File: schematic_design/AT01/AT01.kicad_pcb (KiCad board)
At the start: 2 copper layers, 36 parts, among them J1 JST Connector, J2 Conn_01x04_Pin, M2 Motor_DC (Pump), M3 Motor_DC (Solenoid), P1 USB_C_Plug_USB2.0, Q1 DMG2301L, SW1 SW_Push, U1 MPRLS0025PA00001A, U2 FT232RL, U3 DRV8833PW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

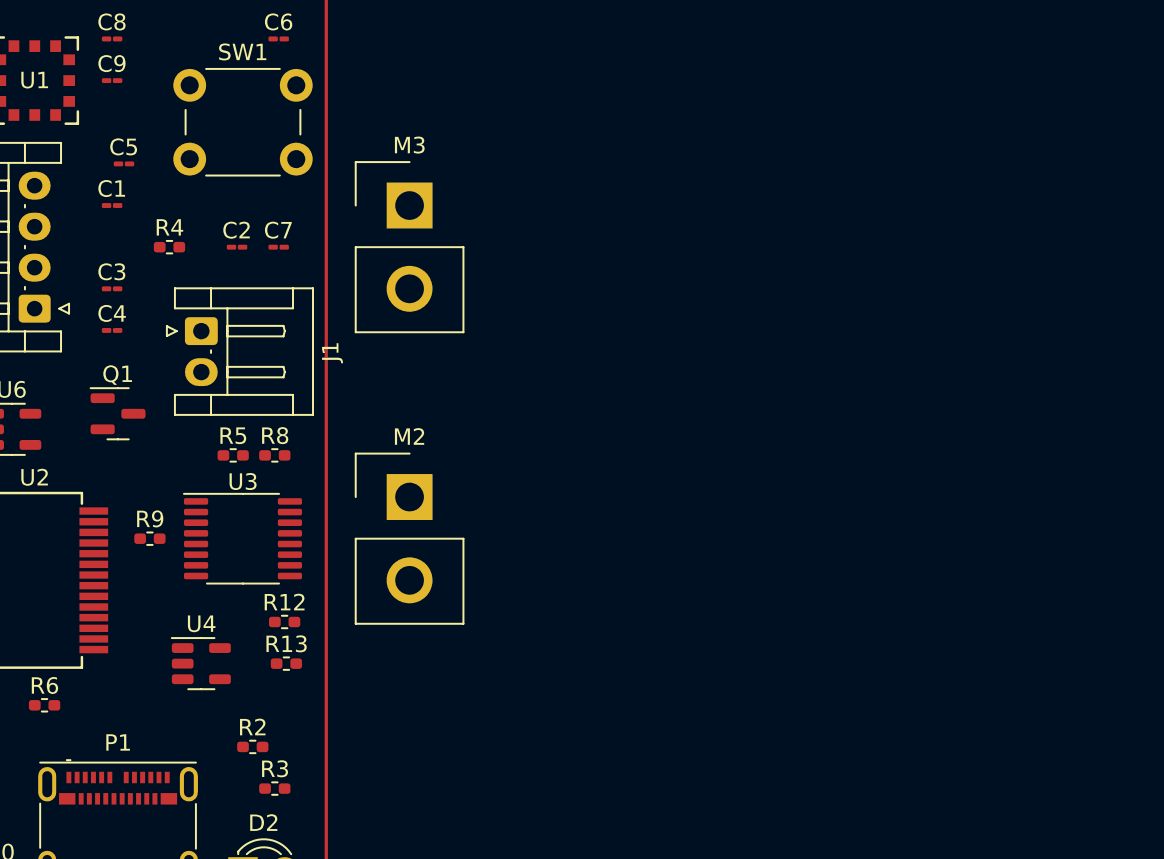
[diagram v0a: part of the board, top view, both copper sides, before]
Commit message: fixing up labels, gnds, added some protection diodes
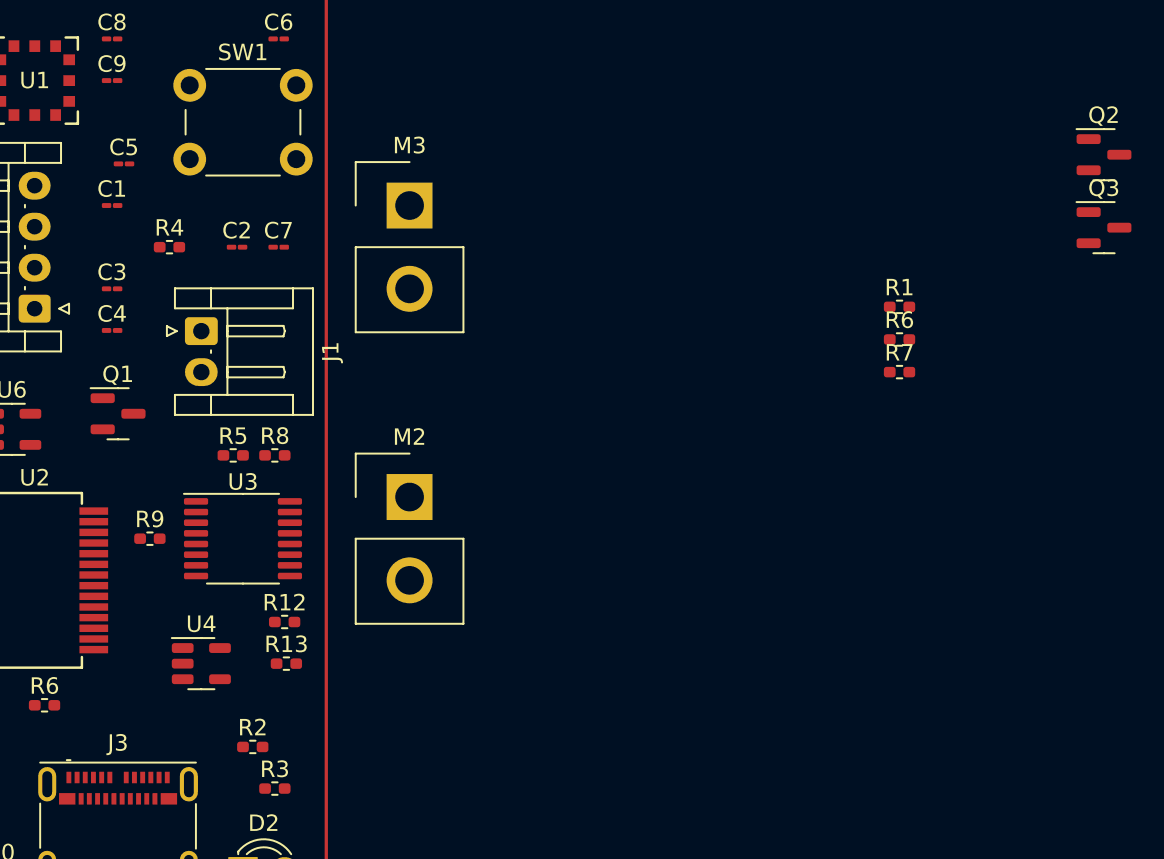
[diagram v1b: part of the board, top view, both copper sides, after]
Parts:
- removed P1: USB_C_Plug_USB2.0, Connector_USB:USB_C_Receptacle_Molex_105450-0101
- added J3: USB_C_Receptacle_USB2.0, Connector_USB:USB_C_Receptacle_Molex_105450-0101, F.Cu at (139.7, 147.3)
- added Q2: 2N7002, Package_TO_SOT_SMD:SOT-23, F.Cu at (199.8, 106.1)
- added Q3: 2N7002, Package_TO_SOT_SMD:SOT-23, F.Cu at (199.8, 110.6)
- added R1: 5.1K, Resistor_SMD:R_0402_1005Metric_Pad0.72x0.64mm_HandSolder, F.Cu at (187.4, 115.4)
- added R6: 5.1K, Resistor_SMD:R_0402_1005Metric_Pad0.72x0.64mm_HandSolder, F.Cu at (187.4, 117.4)
- added R7: 5.1K, Resistor_SMD:R_0402_1005Metric_Pad0.72x0.64mm_HandSolder, F.Cu at (187.4, 119.4)
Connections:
- net +3.3V renamed /3V3
- D1 pad 2: VBUS -> /VBUS
- Q1 pad 1: VBUS -> /VBUS
- R3 pad 1: VBUS -> /VBUS
- U2 pad 20: /VBUS_UART -> /VBUS
- U2 pad 4: /VBUS_UART -> /VBUS
- U4 pad 4: VBUS -> /VBUS

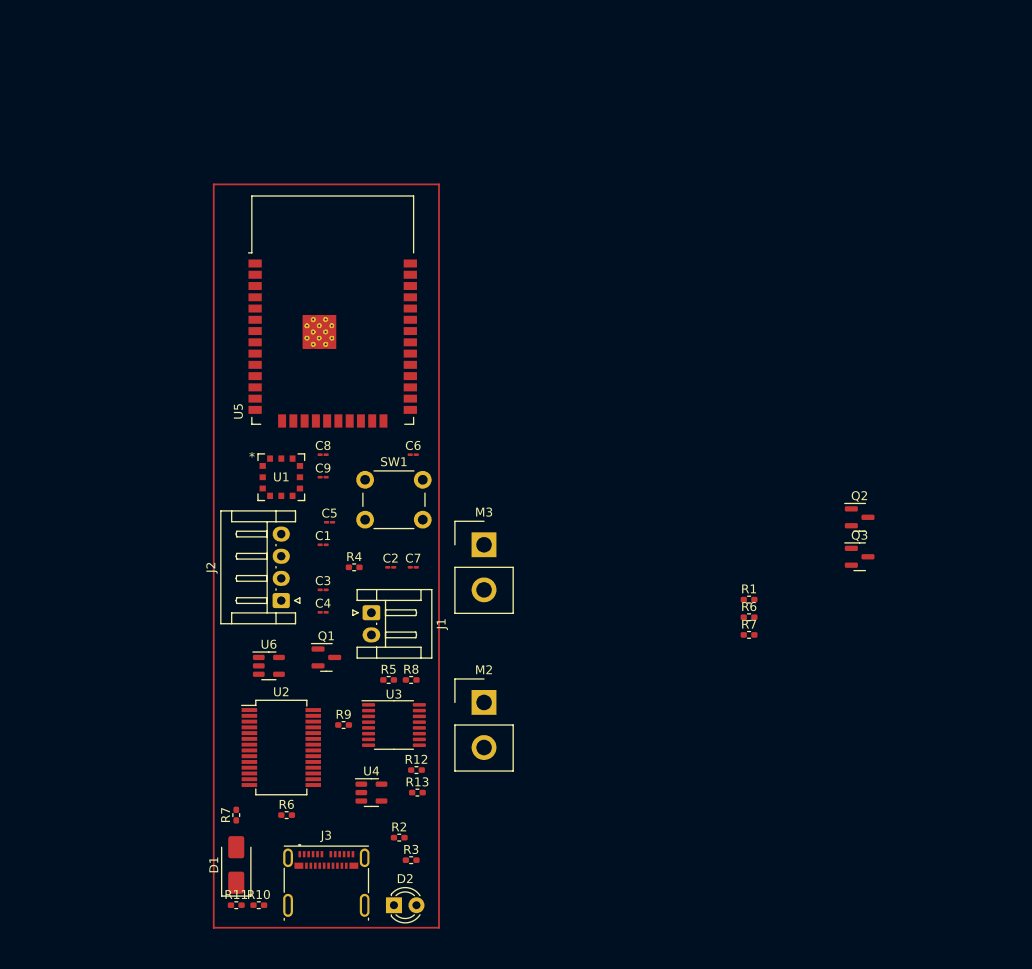
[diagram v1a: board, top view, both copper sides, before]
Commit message: reddit fixes, adding buttons/leds, restarting pcb layout
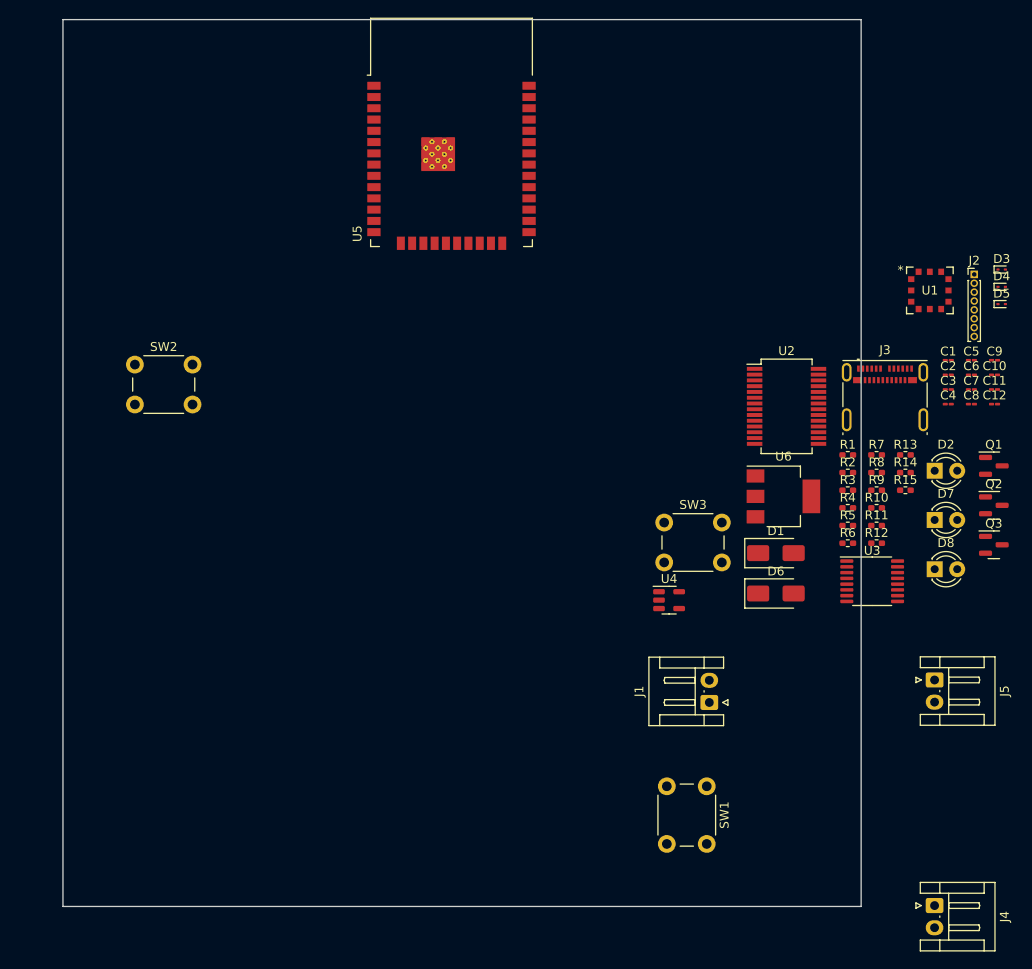
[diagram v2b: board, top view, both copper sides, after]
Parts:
- removed M2: Motor_DC (Pump), Connector_Samtec_HPM_THT:Samtec_HPM-02-05-x-S_Straight_1x02_Pitch5.08mm
- removed M3: Motor_DC (Solenoid), Connector_Samtec_HPM_THT:Samtec_HPM-02-05-x-S_Straight_1x02_Pitch5.08mm
- removed the R6 at (187.4, 117.4)
- removed the R6 at (135.2, 139.7)
- removed the R7 at (187.4, 119.4)
- removed the R7 at (129.5, 139.7)
- added C10: 100uF, Capacitor_SMD:C_01005_0402Metric_Pad0.57x0.30mm_HandSolder, F.Cu at (215.0, 90.1)
- added C11: 10uF, Capacitor_SMD:C_01005_0402Metric_Pad0.57x0.30mm_HandSolder, F.Cu at (215.0, 91.7)
- added C12: 1uF, Capacitor_SMD:C_01005_0402Metric_Pad0.57x0.30mm_HandSolder, F.Cu at (215.0, 93.4)
- added D3: ESD9B3.3ST5G, Diode_SMD:D_SOD-923, F.Cu at (215.8, 78.2)
- added D4: ESD9B3.3ST5G, Diode_SMD:D_SOD-923, F.Cu at (215.8, 80.1)
- added D5: ESD9B3.3ST5G, Diode_SMD:D_SOD-923, F.Cu at (215.8, 82.1)
- added D6: B120-E3, Diode_SMD:D_SMA, F.Cu at (190.4, 114.7)
- added D7: LED, LED_THT:LED_D3.0mm, F.Cu at (208.3, 106.4)
- added D8: LED, LED_THT:LED_D3.0mm, F.Cu at (208.3, 112.0)
- added J4: DC Pump Connector, Connector_JST:JST_EH_S2B-EH_1x02_P2.50mm_Horizontal, F.Cu at (208.3, 149.9)
- added J5: Solenoid Valve Connector, Connector_JST:JST_EH_S2B-EH_1x02_P2.50mm_Horizontal, F.Cu at (208.3, 124.5)
- added R14: 5.1K, Resistor_SMD:R_0402_1005Metric_Pad0.72x0.64mm_HandSolder, F.Cu at (205.0, 101.1)
- added R15: 5.1K, Resistor_SMD:R_0402_1005Metric_Pad0.72x0.64mm_HandSolder, F.Cu at (205.0, 103.1)
- added R6: 5.1K, Resistor_SMD:R_0402_1005Metric_Pad0.72x0.64mm_HandSolder, F.Cu at (198.5, 109.0)
- added R7: 5.1K, Resistor_SMD:R_0402_1005Metric_Pad0.72x0.64mm_HandSolder, F.Cu at (201.7, 99.1)
- added SW2: SW_Push, Button_Switch_THT:SW_PUSH_6mm, F.Cu at (118.1, 88.9)
- added SW3: SW_Push, Button_Switch_THT:SW_PUSH_6mm, F.Cu at (177.8, 106.7)
- C5: value 10uF -> 1uF
- J2: value Conn_01x04_Pin -> Conn_01x08; footprint Connector_JST:JST_EH_S4B-EH_1x04_P2.50mm_Horizontal -> Connector_PinHeader_1.00mm:PinHeader_1x08_P1.00mm_Vertical
- R11: value 100K -> 10K
- R13, R2: value 10K -> 2.2K
- R8: value 5.1K -> 20K
- U6: value AP2112K-3.3 -> LM1117MP-3.3; footprint Package_TO_SOT_SMD:SOT-23-5 -> Package_TO_SOT_SMD:SOT-223-3_TabPin2
- moved J2 86.4 mm to (212.8, 78.7), turned to 0 degrees
- moved R11 83.9 mm to (201.7, 107.0)
- moved J3 83.5 mm to (202.7, 92.6)
- moved R10 82.8 mm to (201.7, 105.1)
- moved Q1 78.3 mm to (215.0, 100.3)
- moved D2 78.2 mm to (208.3, 100.9)
- moved C9 76.8 mm to (215.0, 88.4)
- moved U1 76.1 mm to (207.7, 80.5)
- moved C5 74.6 mm to (212.4, 88.4)
- moved C4 74.3 mm to (209.8, 93.4)
- moved C3 74.0 mm to (209.8, 91.7)
- moved C1 73.5 mm to (209.8, 88.4)
- moved C8 73.3 mm to (212.4, 93.4)
- moved D1 70.3 mm to (190.4, 110.2), turned to 0 degrees
- moved U2 68.7 mm to (191.6, 93.6)
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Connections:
- net /DRV_FAULT renamed DRV_FAULT
- net /DRV_SLEEP renamed DRV_SLEEP
- net /DTR renamed Net-(Q2-S)
- net /GPIO0 renamed GPIO0
- net /MOTOR_PIN_1 renamed MOTOR_PIN_1
- net /MOTOR_PIN_2 renamed MOTOR_PIN_2
- net /RTS renamed Net-(Q3-S)
- net /RXD0 renamed RXD0
- net /SCL renamed SCL
- net /SDA renamed SDA
- net /SOLENOID_PIN_1 renamed SOLENOID_PIN_1
- net /SOLENOID_PIN_2 renamed SOLENOID_PIN_2
- net /TXD0 renamed TXD0
- C1 pad 1: /3V3 -> 3V3
- C4 pad 2: +BATT -> Net-(D6-K)
- C5 pad 1: /RESET -> EN
- C7 pad 2: +BATT -> VBAT
- C9 pad 1: /3V3 -> Net-(U5-IO26)
- D1 pad 2: /VBUS -> VBUS
- J1 pad 1: +BATT -> VBAT
- J2 pad 1: /SCK -> GND
- J2 pad 2: /MOSI -> BL_SCREEN
- J2 pad 3: /MISO -> RST_SCREEN
- J2 pad 4: /IO32_A7 -> DC_SCREEN
- J3 pad A4: /VBUS -> VBUS
- J3 pad A9: /VBUS -> VBUS
- J3 pad B4: /VBUS -> VBUS
- J3 pad B9: /VBUS -> VBUS
- Q1 pad 1: /VBUS -> VBUS
- Q1 pad 3: +BATT -> VBAT
- Q3 pad 3: /EN -> EN
- R11 pad 1: Net-(U6-EN) -> GND
- R11 pad 2: Net-(D1-K) -> Net-(U5-SENSOR_VP)
- R13 pad 1: /3V3 -> 3V3
- R2 pad 1: /3V3 -> 3V3
- R3 pad 1: /VBUS -> VBUS
- R4 pad 1: /3V3 -> 3V3
- R4 pad 2: /RESET -> EN
- R8 pad 1: /VBUS_UART -> Net-(U5-SENSOR_VP)
- R8 pad 2: GND -> VBAT
- SW1 pad 1: /RESET -> EN
- U1 pad 12: /3V3 -> 3V3
- U2 pad 20: /VBUS -> VBUS
- U2 pad 4: /VBUS -> VBUS
- U3 pad 12: +BATT -> Net-(D6-K)
- U4 pad 3: +BATT -> VBAT
- U4 pad 4: /VBUS -> VBUS
- U5 pad 10: /A1_DAC1 -> Net-(U5-IO25)
- U5 pad 11: /A0_DAC2 -> Net-(U5-IO26)
- U5 pad 2: /3V3 -> 3V3
- U5 pad 20: /SCK -> unconnected-(U5-SCK/CLK-Pad20)
- U5 pad 24: /GPIO2 -> Net-(U5-IO2)
- U5 pad 26: /A5_IO4 -> unconnected-(U5-IO4-Pad26)
- U5 pad 27: /IO16 -> Net-(U5-IO16)
- U5 pad 28: /IO17 -> unconnected-(U5-IO17-Pad28)
- U5 pad 29: /SCK -> SCK
- U5 pad 3: /RESET -> EN
- U5 pad 30: /MOSI -> MOSI
- U5 pad 31: /MISO -> unconnected-(U5-IO19-Pad31)
- U5 pad 4: /A4_IO36 -> Net-(U5-SENSOR_VP)
- U5 pad 5: /A3_I39 -> unconnected-(U5-SENSOR_VN-Pad5)
- U5 pad 6: /A2_I34 -> RST_SCREEN
- U5 pad 7: /A13_I35 -> BL_SCREEN
- U5 pad 8: /IO32_A7 -> CS
- U5 pad 9: /IO33_A9 -> DC_SCREEN
- U6 pad 1: Net-(D1-K) -> GND
- U6 pad 2: GND -> 3V3
- U6 pad 3: Net-(U6-EN) -> Net-(D1-K)
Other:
- board outline added: 90 x 100 mm

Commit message: initial layout revision
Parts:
- added C13: 10uF, Capacitor_SMD:C_1206_3216Metric_Pad1.33x1.80mm_HandSolder, F.Cu at (148.0, 89.5)
- added H1: MountingHole, MountingHole:MountingHole_2.2mm_M2_ISO7380, F.Cu at (108.4, 76.4)
- added H2: MountingHole, MountingHole:MountingHole_2.2mm_M2_ISO7380, F.Cu at (108.5, 124.7)
- added H3: MountingHole, MountingHole:MountingHole_2.2mm_M2_ISO7380, F.Cu at (186.4, 124.5)
- added H4: MountingHole, MountingHole:MountingHole_2.2mm_M2_ISO7380, F.Cu at (167.4, 76.3)
- C1, C10, C11, C12, C2, C3, C4, C5, C6, C7, C8, C9: footprint Capacitor_SMD:C_01005_0402Metric_Pad0.57x0.30mm_HandSolder -> Capacitor_SMD:C_0402_1005Metric_Pad0.74x0.62mm_HandSolder
- J3: footprint Connector_USB:USB_C_Receptacle_Molex_105450-0101 -> Connector_USB:USB_C_Receptacle_HRO_TYPE-C-31-M-12
- U5: footprint RF_Module:ESP32-WROOM-32D -> RF_Module:ESP32-WROOM-32U
- moved J4 109.1 mm to (112.4, 97.8), turned to 90 degrees
- moved J5 96.5 mm to (112.4, 113.5), turned to 90 degrees
- moved C11 95.3 mm to (120.6, 104.5)
- moved C4 93.1 mm to (118.5, 111.4), turned to 90 degrees
- moved C3 91.4 mm to (123.2, 121.0), turned to 90 degrees
- moved J2 88.9 mm to (127.0, 102.0)
- moved R12 81.1 mm to (120.6, 108.1)
- moved C12 80.5 mm to (140.0, 122.6), turned to -90 degrees
- moved U3 79.0 mm to (122.3, 113.0), turned to -90 degrees
- moved R11 75.2 mm to (128.0, 92.1), turned to 90 degrees
- moved R8 74.9 mm to (128.0, 88.1), turned to 90 degrees
- moved D6 72.5 mm to (123.0, 88.1), turned to 90 degrees
- moved C10 72.0 mm to (143.0, 90.1), turned to 90 degrees
- moved C5 69.4 mm to (143.0, 87.5)
- moved D7 66.4 mm to (145.0, 126.5), turned to 90 degrees
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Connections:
- C9 pad 1: Net-(U5-IO26) -> Net-(U5-IO21)
- J2 pad 2: BL_SCREEN -> RST_SCREEN
- J2 pad 3: RST_SCREEN -> BL_SCREEN
- J2 pad 4: DC_SCREEN -> CS
- J2 pad 5: CS -> DC_SCREEN
- SW2 pad 1: Net-(U5-IO26) -> Net-(U5-IO21)
- U5 pad 11: Net-(U5-IO26) -> DRV_SLEEP
- U5 pad 12: DRV_SLEEP -> DRV_FAULT
- U5 pad 33: DRV_FAULT -> Net-(U5-IO21)
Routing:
- net 3V3: track 0.00 -> 88.4 mm, vias 0 -> 4
- net VBAT: track 0.00 -> 81.7 mm
- net EN: track 0.00 -> 59.3 mm, vias 0 -> 2
- net VBUS: track 0.00 -> 57.6 mm
- net Net-(D6-K): track 0.00 -> 36.0 mm, vias 0 -> 2
- net Net-(U5-IO21): track 0.00 -> 28.8 mm, vias 0 -> 1
- net Net-(D1-K): track 0.00 -> 28.1 mm, vias 0 -> 2
- net SOLENOID_PIN_2: track 0.00 -> 26.8 mm
- net SCK: track 0.00 -> 23.9 mm, vias 0 -> 2
- net Net-(U5-IO25): track 0.00 -> 23.7 mm, vias 0 -> 1
- net MOSI: track 0.00 -> 22.6 mm, vias 0 -> 2
- net TXD0: track 0.00 -> 21.3 mm, vias 0 -> 2
- net Net-(J4-Pin_2): track 0.00 -> 20.7 mm, vias 0 -> 2
- net Net-(J4-Pin_1): track 0.00 -> 19.1 mm, vias 0 -> 1
- net RXD0: track 0.00 -> 19.0 mm
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- added copper zone on F.Cu, net GND
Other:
- board size 90 x 100 mm -> 85 x 56 mm
- board text added: "AT01 Rev 1.0"
- board text added: "Designed by: Diana Temelkos Hassan Khan Haashim Shahzada Sayeed Hasan"

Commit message: DRC fixes
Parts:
- moved R12 6.48 mm to (115.5, 104.1), turned to -90 degrees
- moved D3 2.40 mm to (178.4, 114.0)
- moved D5 1.70 mm to (178.3, 103.9)
- moved D4 1.30 mm to (178.3, 108.3)
- moved C1 1.28 mm to (160.2, 90.0)
- moved R4 1.22 mm to (135.0, 93.7)
- moved C6 0.30 mm to (172.4, 113.3)
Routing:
- net GND: track 12.0 -> 22.7 mm, vias 3 -> 8
- net VBUS: track 57.6 -> 66.2 mm, vias 0 -> 4
- net Net-(U3-AISEN): track 6.88 -> 13.9 mm, vias 2 -> 4
- net 3V3: track 88.4 -> 94.7 mm, vias 4 -> 10
- net Net-(D3-A2): track 14.1 -> 17.8 mm
- net Net-(J3-CC2): track 7.56 -> 10.8 mm, vias 0 -> 2
- net Net-(D4-A2): track 11.3 -> 12.1 mm
- net EN: track 59.3 -> 59.6 mm, vias 2 -> 4
- net Net-(J3-CC1): track 8.77 -> 8.89 mm, vias 0 -> 2
- net VBAT: vias 0 -> 4

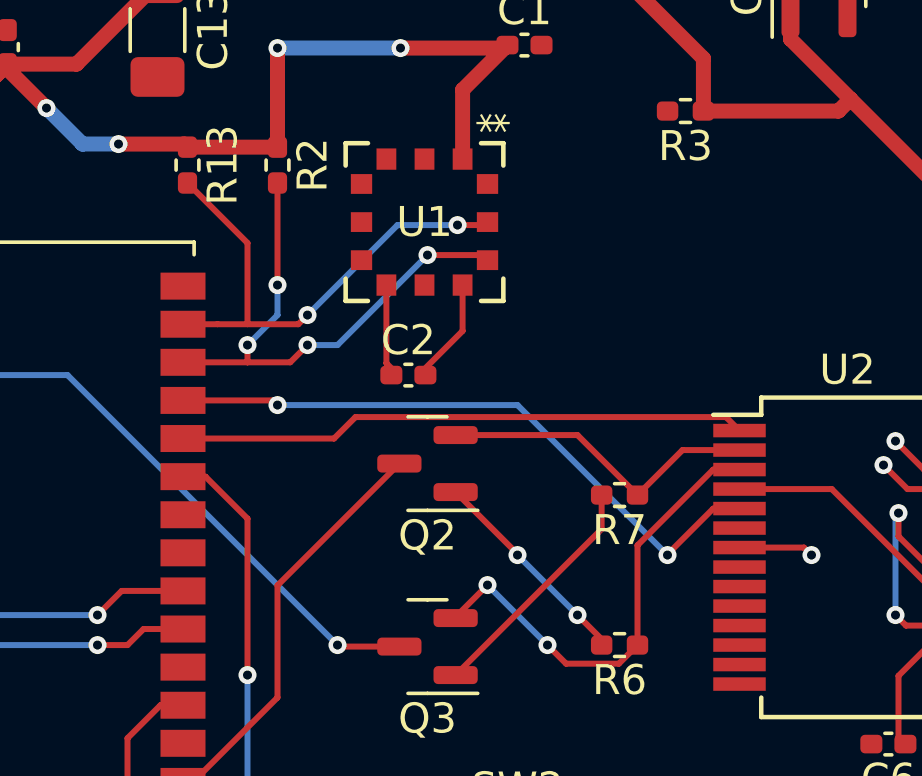
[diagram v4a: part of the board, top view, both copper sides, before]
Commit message: updated incorrect UART pins
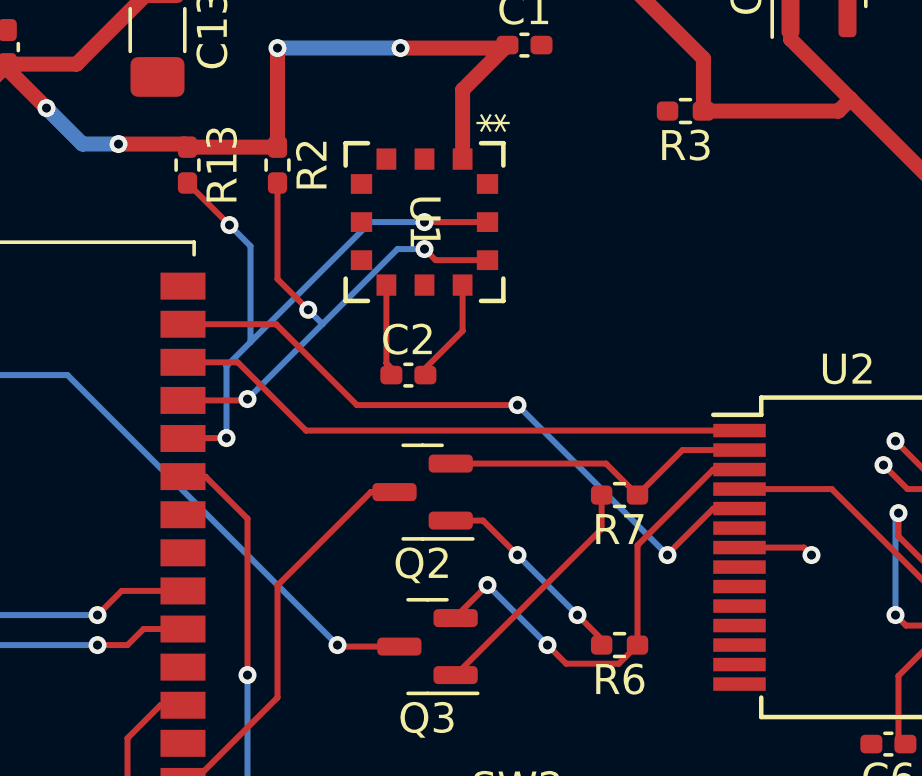
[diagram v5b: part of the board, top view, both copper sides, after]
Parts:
- moved Q2 0.96 mm to (156.8, 104.9)
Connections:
- U5 pad 34: RXD0 -> SDA
- U5 pad 35: TXD0 -> SCL
- U5 pad 36: SCL -> RXD0
- U5 pad 37: SDA -> TXD0
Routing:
- net SDA: track 17.1 -> 20.9 mm, vias 2 -> 3
- net TXD0: track 21.3 -> 22.4 mm
- net GPIO0: track 13.8 -> 13.2 mm
- net SCL: track 18.1 -> 18.0 mm, vias 4 -> 3
